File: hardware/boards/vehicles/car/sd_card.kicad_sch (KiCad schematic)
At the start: 4 parts, among them J10 Conn_02x03_Odd_Even

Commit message: REFACTO relinked every kicad projects
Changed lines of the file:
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@@
 	)
 	(no_connect
-		(at 184.15 95.25)
+		(at 185.42 97.79)
 	)
 	(wire
@@
 	(symbol
 		(lib_id "air_sens_lib:SD_SLOT")
-		(at 171.45 99.06 0)
+		(at 147.32 96.52 270)
 		(unit 1)
 		(exclude_from_sim no)
@@
 		(dnp no)
 		(property "Reference" "SD1"
-			(at 178.308 107.188 0)
+			(at 176.784 106.172 90)
 			(effects
 				(font
@@
 		)
 		(property "Value" "~"
-			(at 171.45 86.36 0)
+			(at 160.02 96.52 0)
 			(effects
 				(font
@@
 		)
 		(property "Footprint" "air_sens_foots:SD_SLOT"
-			(at 171.196 110.744 0)
+			(at 135.636 96.266 0)
 			(effects
 				(font
@@
 		)
 		(property "Datasheet" ""
-			(at 171.45 99.06 0)
+			(at 147.32 96.52 0)
 			(effects
 				(font
@@
 		)
 		(property "Description" ""
-			(at 171.45 99.06 0)
+			(at 147.32 96.52 0)
 			(effects
 				(font
@@
 		(pin "9"
 		)
-		(pin "11"
-		)
 		(pin "2"
 		)
-		(pin "14"
-		)
 		(pin "1"
 		)
@@
 		(pin "8"
 		)
-		(pin "10"
-		)
-		(pin "12"
-		)
-		(pin "13"
-		)
 		(instances

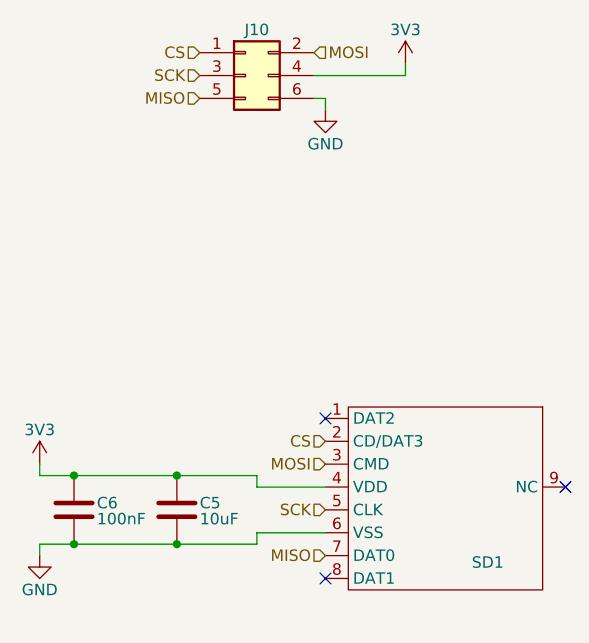
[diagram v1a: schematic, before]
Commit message: updated main points of the car schematic
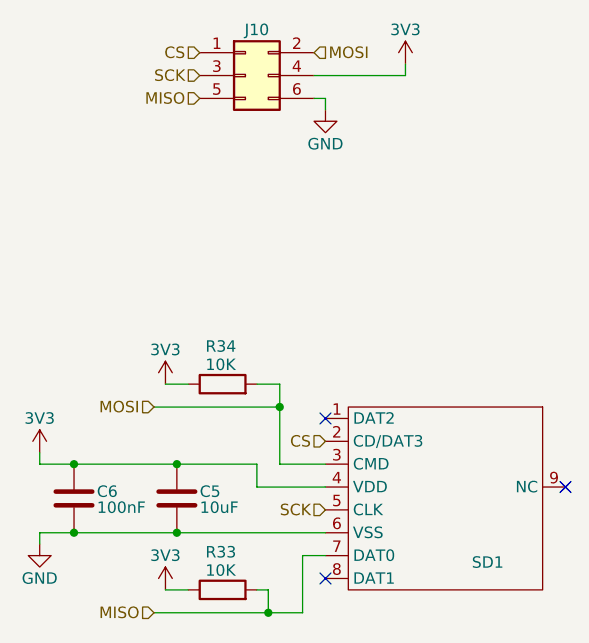
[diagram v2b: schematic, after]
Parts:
- added R33, R34: 10K, Resistor_SMD:R_0603_1608Metric_Pad0.98x0.95mm_HandSolder, symbol Device:R
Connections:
- net 3V3: now also R33.1, R34.1
- net MISO: now also R33.2
- net MOSI: now also R34.2
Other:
- moved on the sheet: C5, C6

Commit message: car PCB
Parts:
- removed J10: Conn_02x03_Odd_Even, Connector_PinHeader_2.54mm:PinHeader_2x03_P2.54mm_Vertical, symbol Connector_Generic:Conn_02x03_Odd_Even
- SD1: value ~ -> SD Card Slot
- renumbered C6 to C18, C5 to C19, R34 to R13, R33 to R14

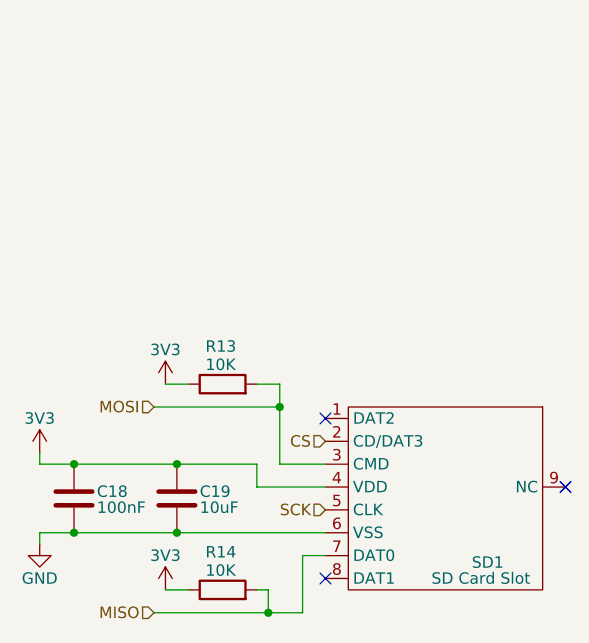
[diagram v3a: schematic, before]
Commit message: change kicad default to custom
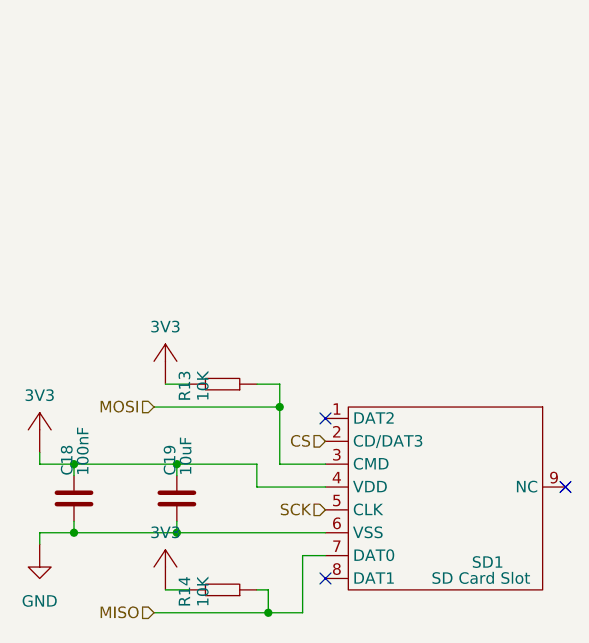
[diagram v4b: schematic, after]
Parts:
- C18, C19: footprint Capacitor_SMD:C_0603_1608Metric_Pad1.08x0.95mm_HandSolder -> common:C_0603; symbol Device:C -> common:Capacitor
- R13, R14: footprint Resistor_SMD:R_0603_1608Metric_Pad0.98x0.95mm_HandSolder -> common:R_0603; symbol Device:R -> common:Resistor
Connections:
- net 3V3: now also C18.2, C19.2, R13.2, R14.2; no longer C18.1, C19.1, R13.1, R14.1
- net GND: now also C18.1, C19.1; no longer C18.2, C19.2
- net MISO: now also R14.1; no longer R14.2
- net MOSI: now also R13.1; no longer R13.2
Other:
- moved on the sheet: C18, C19, R13, R14
